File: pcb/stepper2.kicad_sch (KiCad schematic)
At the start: 41 parts, among them J1 DE15_Receptacle_HighDensity, J2 DE15_Receptacle_HighDensity, J3 DE15_Receptacle_HighDensity, J4 DA15_Receptacle_MountingHoles, J5 DA15_Receptacle_MountingHoles, J6 DA15_Receptacle_MountingHoles, SW1 SW_Push, U4 TMC2209_BIGTREETECH, U5 TMC2209_BIGTREETECH, U6 TMC2209_BIGTREETECH, U7 AM26LS32Ax, U8 AM26LS32ACN, U9 AM26LS32ACN

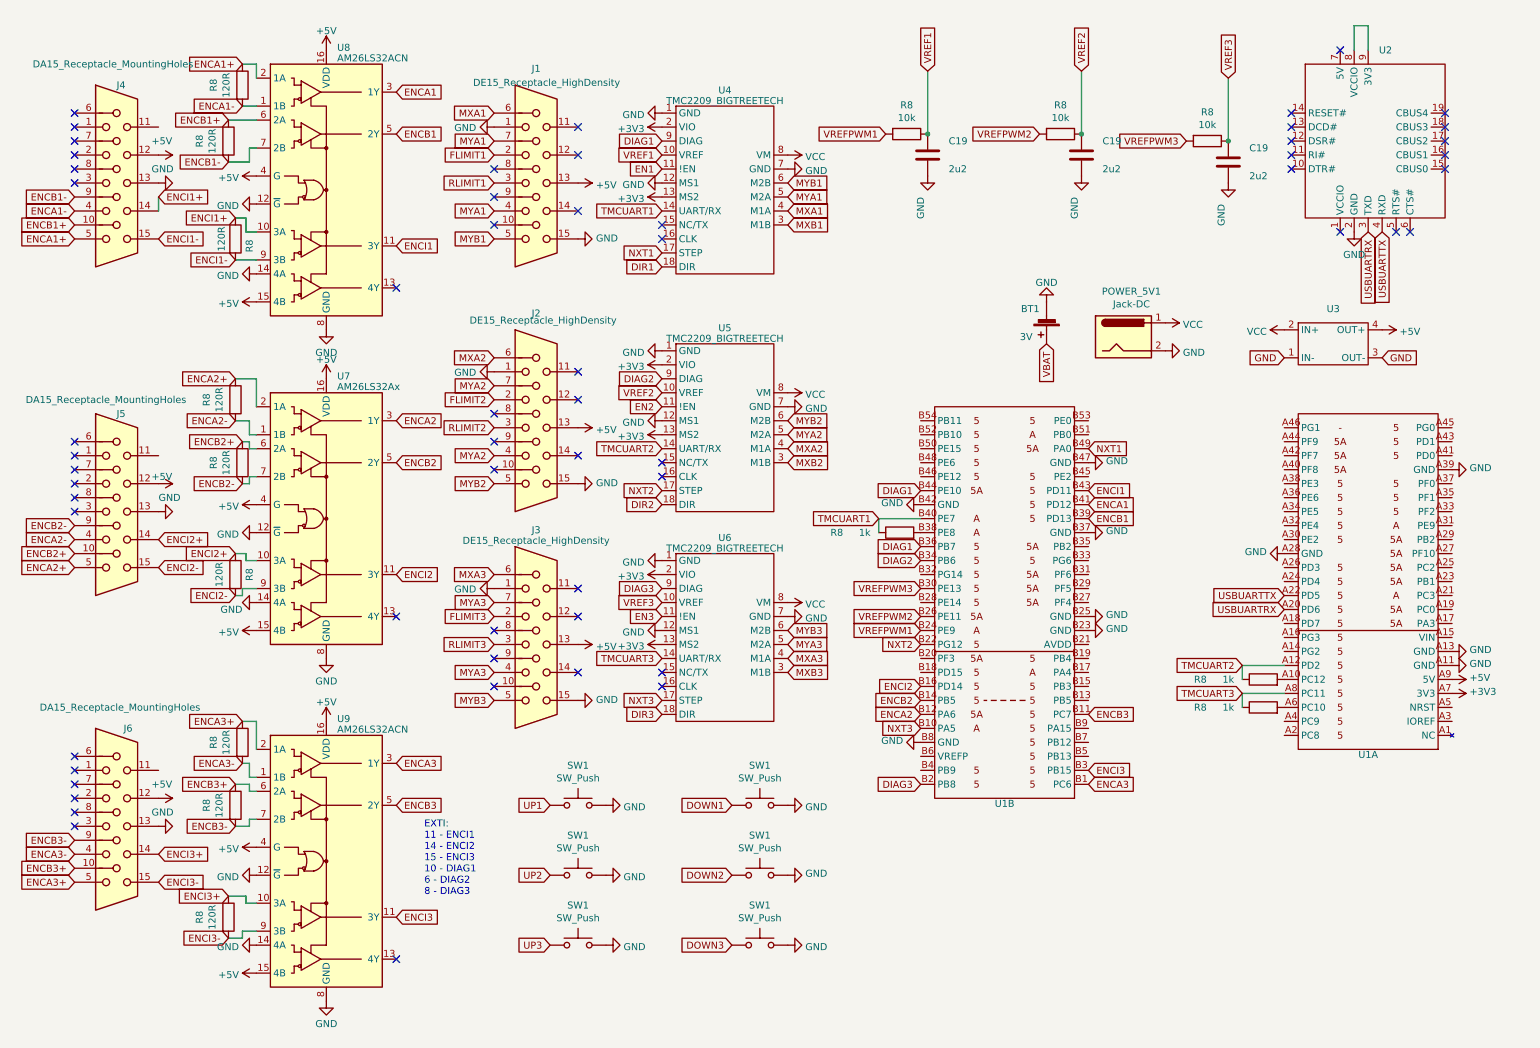
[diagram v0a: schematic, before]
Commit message: added 4, 5, 6, 7 pin JST connectors
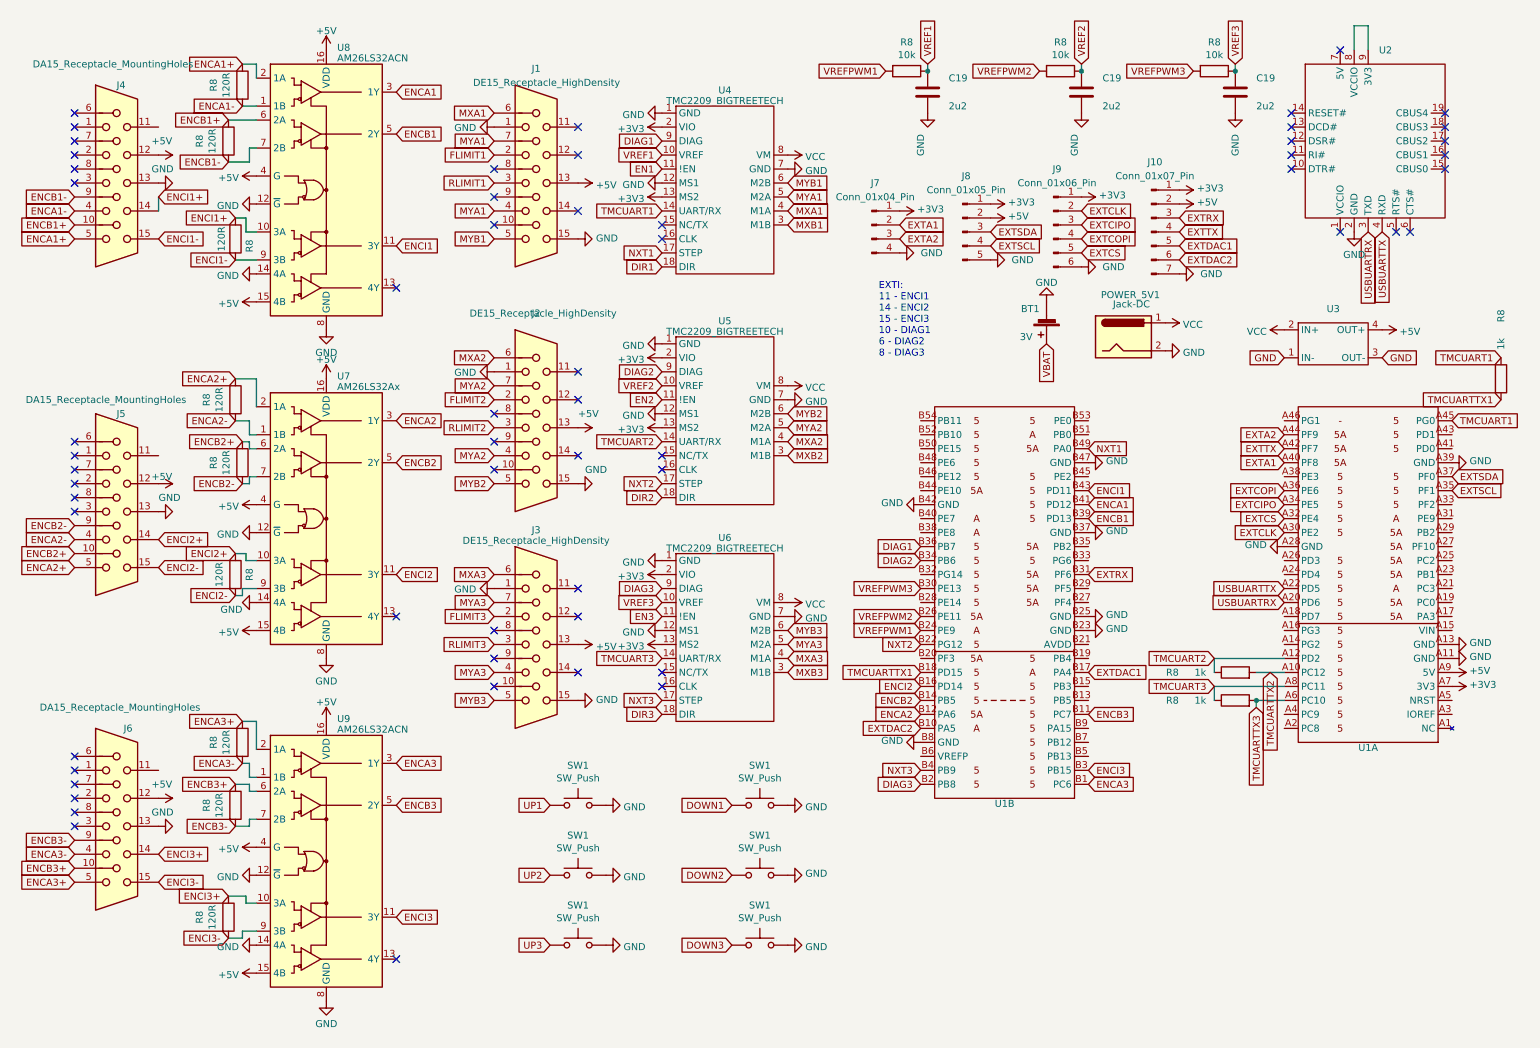
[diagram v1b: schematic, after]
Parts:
- added J10: Conn_01x07_Pin, symbol Connector:Conn_01x07_Pin
- added J7: Conn_01x04_Pin, symbol Connector:Conn_01x04_Pin
- added J8: Conn_01x05_Pin, symbol Connector:Conn_01x05_Pin
- added J9: Conn_01x06_Pin, symbol Connector:Conn_01x06_Pin
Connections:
- net +3V3: now also J10.1 (Pin_1), J7.1 (Pin_1), J8.1 (Pin_1), J9.1 (Pin_1)
- net +5V: now also J10.2 (Pin_2), J8.2 (Pin_2)
- net DIAG1: no longer U1.B44 (PE10)
- net GND: now also J10.7 (Pin_7), J7.4 (Pin_4), J8.5 (Pin_5), J9.6 (Pin_6)
- net NXT3: now also U1.B4 (PB9); no longer U1.B10 (PA5)
- net TMCUART1: now also U1.A45 (PG0); no longer U1.B40 (PE7)
- net TMCUARTTX2: now reaches R8.2, U1.A10 (PC12)
- net EXTCLK: now reaches U1.A30 (PE2)
- net EXTCLK: now also J9.2 (Pin_2)
- net EXTCS: now reaches U1.A32 (PE4)
- net EXTCS: now also J9.5 (Pin_5)
- net EXTCIPO: now reaches U1.A34 (PE5)
- net EXTCIPO: now also J9.3 (Pin_3)
- net EXTSCL: now reaches U1.A35 (PF1)
- net EXTSCL: now also J8.4 (Pin_4)
- net EXTCOPI: now reaches U1.A36 (PE6)
- net EXTCOPI: now also J9.4 (Pin_4)
- net EXTSDA: now reaches U1.A37 (PF0)
- net EXTSDA: now also J8.3 (Pin_3)
- net EXTA1: now reaches U1.A40 (PF8)
- net EXTA1: now also J7.2 (Pin_2)
- net EXTTX: now reaches U1.A42 (PF7)
- net EXTTX: now also J10.4 (Pin_4)
- net EXTA2: now reaches U1.A44 (PF9)
- net EXTA2: now also J7.3 (Pin_3)
- net TMCUARTTX3: now reaches R8.2, U1.A6 (PC10)
- net at U1.B38 (PE8): no longer R8.2
- net EXTDAC1: now reaches U1.B17 (PA4)
- net EXTDAC1: now also J10.5 (Pin_5)
- net TMCUARTTX1: now reaches U1.B18 (PD15)
- net TMCUARTTX1: now also R8.2
- net EXTRX: now reaches U1.B31 (PF6)
- net EXTRX: now also J10.3 (Pin_3)
- new net EXTDAC2: J10.6 (Pin_6), U1.B10 (PA5)
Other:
- moved on the sheet: C19, R8, U1A, U5

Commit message: PCB - added VBAT; JST peripherial connectors; power supply capacitors
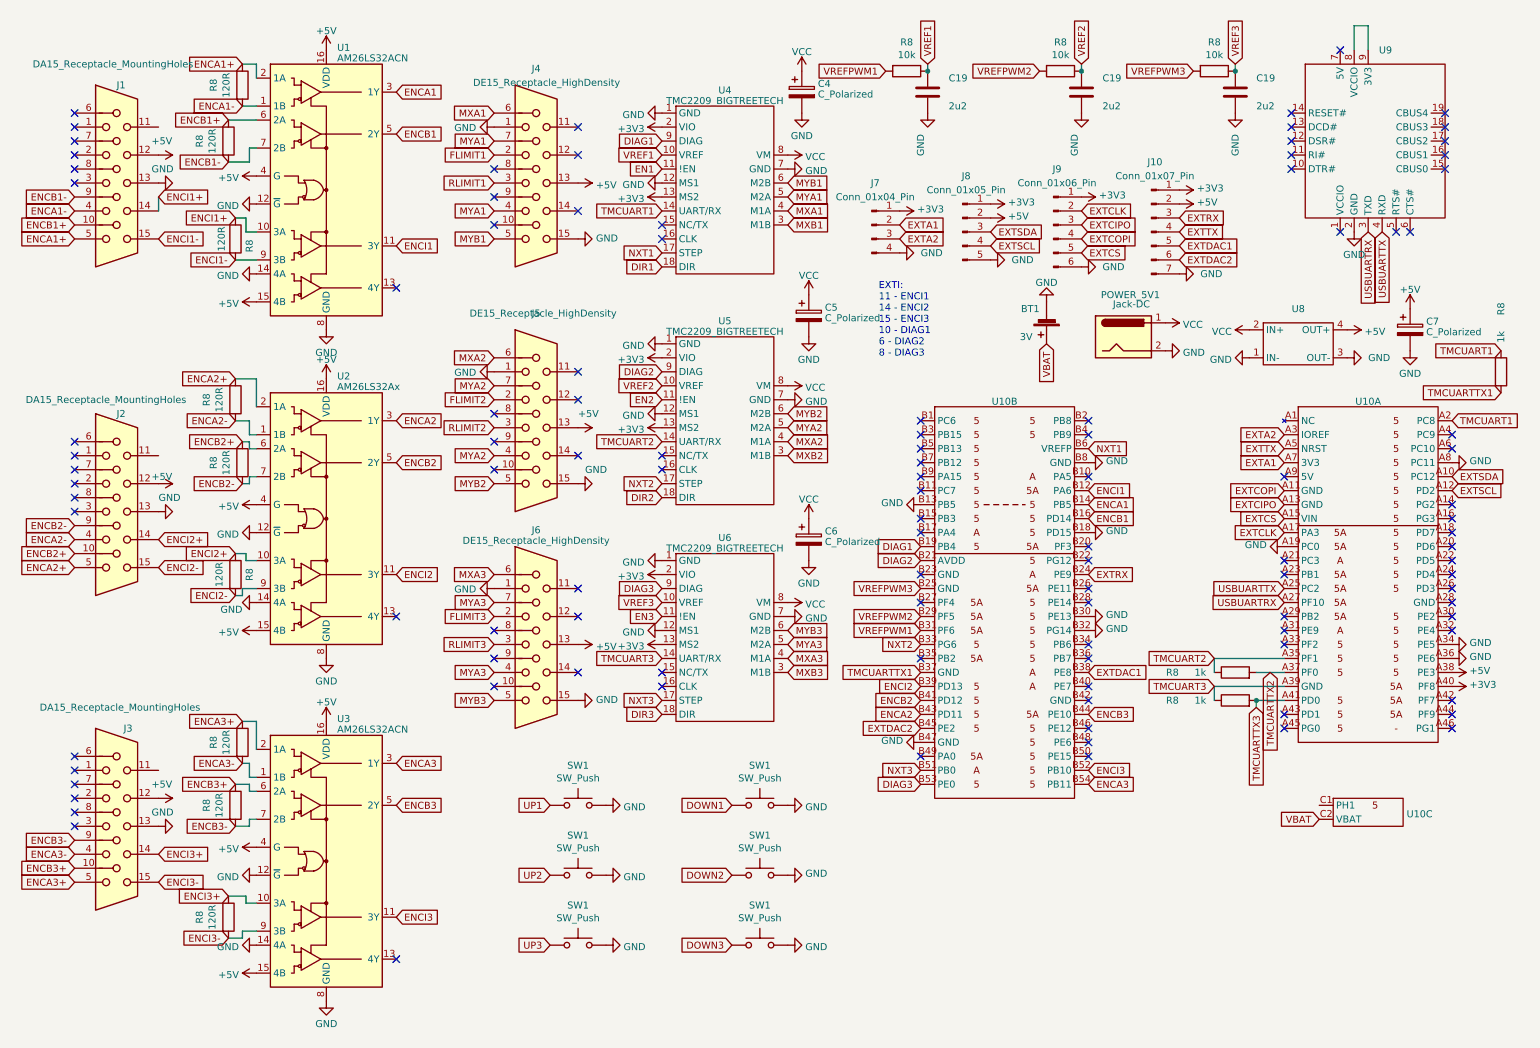
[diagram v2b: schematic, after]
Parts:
- removed U1: ~, stepper2:Nucleo144_H723, symbol stepper5:NucleoH723
- added C4, C5, C6: C_Polarized, Capacitor_SMD:CP_Elec_10x10.5, symbol Device:C_Polarized
- added C7: C_Polarized, Capacitor_SMD:CP_Elec_8x10.5, symbol Device:C_Polarized
- added U10: ~, stepper2:Nucleo144_H723_withVBAT, symbol stepper2:NucleoH723
- J10: footprint (none) -> stepper2:JST_PH_S7B-PH-SM4-TB_1x07-1MP_P2.00mm_Horizontal
- J7: footprint (none) -> stepper2:JST_PH_S4B-PH-SM4-TB_1x04-1MP_P2.00mm_Horizontal
- J8: footprint (none) -> stepper2:JST_PH_S5B-PH-SM4-TB_1x05-1MP_P2.00mm_Horizontal
- J9: footprint (none) -> stepper2:JST_PH_S6B-PH-SM4-TB_1x06-1MP_P2.00mm_Horizontal
- renumbered J4 to J1, J5 to J2, J6 to J3, J1 to J4, J2 to J5, J3 to J6, U8 to U1, U7 to U2, U9 to U3, U3 to U8, U2 to U9
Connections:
- net +3V3: now also U10.A40 (PF8)
- net +5V: now also C7.1, U10.A38 (PE3)
- net DIAG1: now also U10.B19 (PB4)
- net DIAG2: now also U10.B21 (AVDD)
- net DIAG3: now also U10.B53 (PE0)
- net ENCA1: now also U10.B14 (PB5)
- net ENCA2: now also U10.B43 (PD11)
- net ENCA3: now also U10.B54 (PB11)
- net ENCB1: now also U10.B16 (PD14)
- net ENCB2: now also U10.B41 (PD12)
- net ENCB3: now also U10.B44 (PE10)
- net ENCI1: now also U10.B12 (PA6)
- net ENCI2: now also U10.B39 (PD13)
- net ENCI3: now also U10.B52 (PB10)
- net EXTA1: now also U10.A7 (3V3)
- net EXTA2: now also U10.A3 (IOREF)
- net EXTCIPO: now also U10.A13 (GND)
- net EXTCLK: now also U10.A17 (PA3)
- net EXTCOPI: now also U10.A11 (GND)
- net EXTCS: now also U10.A15 (VIN)
- net EXTDAC1: now also U10.B38 (PE8)
- net EXTDAC2: now also U10.B45 (PE2)
- net EXTRX: now also U10.B24 (PE9)
- net EXTSCL: now also U10.A12 (PD2)
- net EXTSDA: now also U10.A10 (PC12)
- net EXTTX: now also U10.A5 (NRST)
- net GND: now also C4.2, C5.2, C6.2, C7.2, U10.A19 (PC0), U10.A34 (PE5), U10.A36 (PE6), U10.A8 (PC11), U10.B13 (PB5), U10.B18 (PD15), U10.B30 (PE13), U10.B32 (PG14), U10.B47 (GND), U10.B8 (GND)
- net NXT1: now also U10.B6 (VREFP)
- net NXT2: now also U10.B33 (PG6)
- net NXT3: now also U10.B51 (PB0)
- net TMCUART1: now also U10.A2 (PC8)
- net TMCUART2: now also U10.A35 (PF1)
- net TMCUART3: now also U10.A39 (GND)
- net TMCUARTTX1: now also U10.B37 (GND)
- net TMCUARTTX2: now also U10.A37 (PF0)
- net TMCUARTTX3: now also U10.A41 (PD0)
- net USBUARTRX: now also U10.A27 (PF10)
- net USBUARTTX: now also U10.A25 (PC2)
- net VBAT: now also U10.C2 (VBAT)
- net VCC: now also C4.1, C5.1, C6.1
- net VREFPWM1: now also U10.B31 (PF6)
- net VREFPWM2: now also U10.B29 (PF5)
- net VREFPWM3: now also U10.B25 (GND)
- no-connect marks 59 -> 108
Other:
- moved on the sheet: R8, U8

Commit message: tweaks in PCB and fixed rotated nucleo parts in schematic
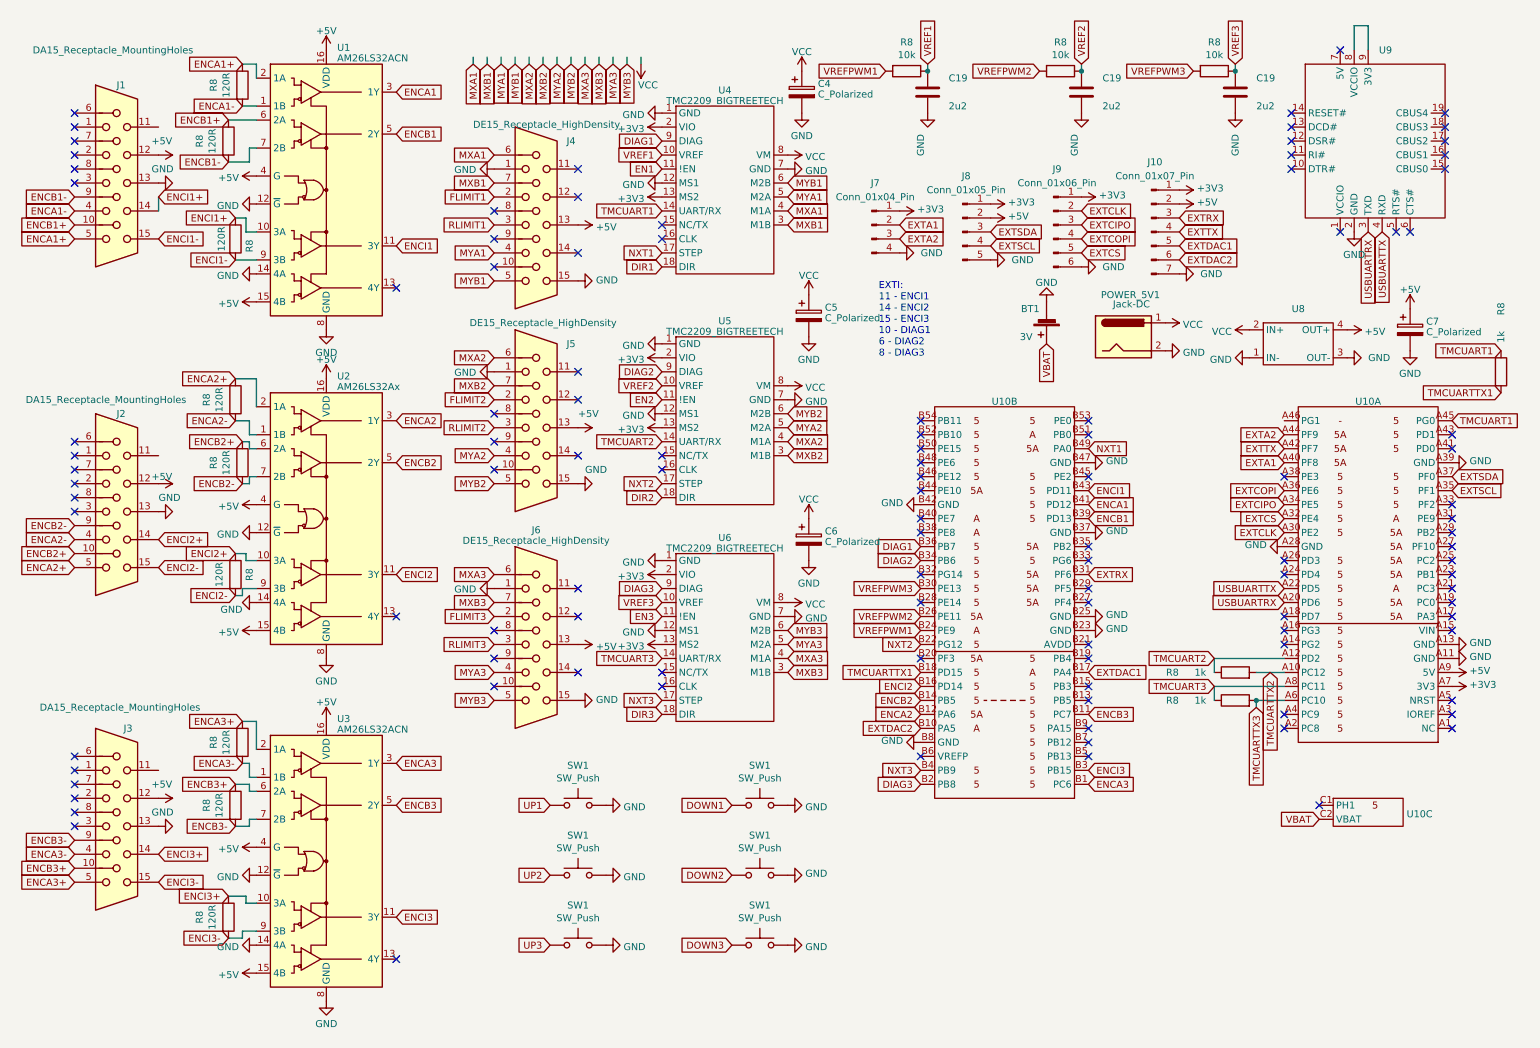
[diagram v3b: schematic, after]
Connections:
- net +3V3: now also U10.A7 (3V3); no longer U10.A40 (PF8)
- net +5V: now also U10.A9 (5V); no longer U10.A38 (PE3)
- net DIAG1: now also U10.B36 (PB7); no longer U10.B19 (PB4)
- net DIAG2: now also U10.B34 (PB6); no longer U10.B21 (AVDD)
- net DIAG3: now also U10.B2 (PB8); no longer U10.B53 (PE0)
- net ENCA1: now also U10.B41 (PD12); no longer U10.B14 (PB5)
- net ENCA2: now also U10.B12 (PA6); no longer U10.B43 (PD11)
- net ENCA3: now also U10.B1 (PC6); no longer U10.B54 (PB11)
- net ENCB1: now also U10.B39 (PD13); no longer U10.B16 (PD14)
- net ENCB2: now also U10.B14 (PB5); no longer U10.B41 (PD12)
- net ENCB3: now also U10.B11 (PC7); no longer U10.B44 (PE10)
- net ENCI1: now also U10.B43 (PD11); no longer U10.B12 (PA6)
- net ENCI2: now also U10.B16 (PD14); no longer U10.B39 (PD13)
- net ENCI3: now also U10.B3 (PB15); no longer U10.B52 (PB10)
- net EXTA1: now also U10.A40 (PF8); no longer U10.A7 (3V3)
- net EXTA2: now also U10.A44 (PF9); no longer U10.A3 (IOREF)
- net EXTCIPO: now also U10.A34 (PE5); no longer U10.A13 (GND)
- net EXTCLK: now also U10.A30 (PE2); no longer U10.A17 (PA3)
- net EXTCOPI: now also U10.A36 (PE6); no longer U10.A11 (GND)
- net EXTCS: now also U10.A32 (PE4); no longer U10.A15 (VIN)
- net EXTDAC1: now also U10.B17 (PA4); no longer U10.B38 (PE8)
- net EXTDAC2: now also U10.B10 (PA5); no longer U10.B45 (PE2)
- net EXTRX: now also U10.B31 (PF6); no longer U10.B24 (PE9)
- net EXTSCL: now also U10.A35 (PF1); no longer U10.A12 (PD2)
- net EXTSDA: now also U10.A37 (PF0); no longer U10.A10 (PC12)
- net EXTTX: now also U10.A42 (PF7); no longer U10.A5 (NRST)
- net GND: now also U10.A11 (GND), U10.A13 (GND), U10.A28 (GND), U10.A39 (GND), U10.B23 (GND), U10.B25 (GND), U10.B37 (GND), U10.B42 (GND); no longer U10.A19 (PC0), U10.A34 (PE5), U10.A36 (PE6), U10.A8 (PC11), U10.B13 (PB5), U10.B18 (PD15), U10.B30 (PE13), U10.B32 (PG14)
- net MXB1: now also J4.7
- net MXB2: now also J5.7
- net MXB3: now also J6.7
- net MYA1: no longer J4.7
- net MYA2: no longer J5.7
- net MYA3: no longer J6.7
- net NXT1: now also U10.B49 (PA0); no longer U10.B6 (VREFP)
- net NXT2: now also U10.B22 (PG12); no longer U10.B33 (PG6)
- net NXT3: now also U10.B4 (PB9); no longer U10.B51 (PB0)
- net TMCUART1: now also U10.A45 (PG0); no longer U10.A2 (PC8)
- net TMCUART2: now also U10.A12 (PD2); no longer U10.A35 (PF1)
- net TMCUART3: now also U10.A8 (PC11); no longer U10.A39 (GND)
- net TMCUARTTX1: now also U10.B18 (PD15); no longer U10.B37 (GND)
- net TMCUARTTX2: now also U10.A10 (PC12); no longer U10.A37 (PF0)
- net TMCUARTTX3: now also U10.A6 (PC10); no longer U10.A41 (PD0)
- net USBUARTRX: now also U10.A20 (PD6); no longer U10.A27 (PF10)
- net USBUARTTX: now also U10.A22 (PD5); no longer U10.A25 (PC2)
- net VREFPWM1: now also U10.B24 (PE9); no longer U10.B31 (PF6)
- net VREFPWM2: now also U10.B26 (PE11); no longer U10.B29 (PF5)
- net VREFPWM3: now also U10.B30 (PE13); no longer U10.B25 (GND)
- no-connect marks 108 -> 109
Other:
- moved on the sheet: J4, U10A, U10B
